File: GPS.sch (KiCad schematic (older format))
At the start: 2 parts

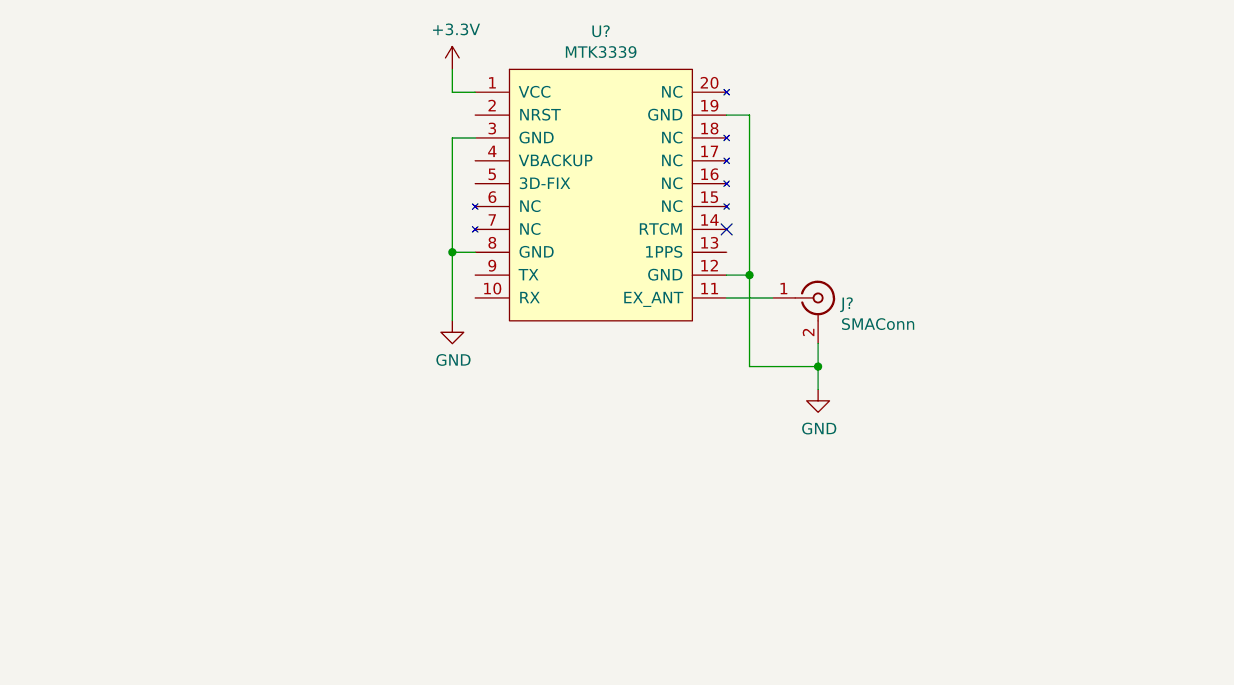
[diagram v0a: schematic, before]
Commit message: Adds connects all modules except for LEDs in schematics
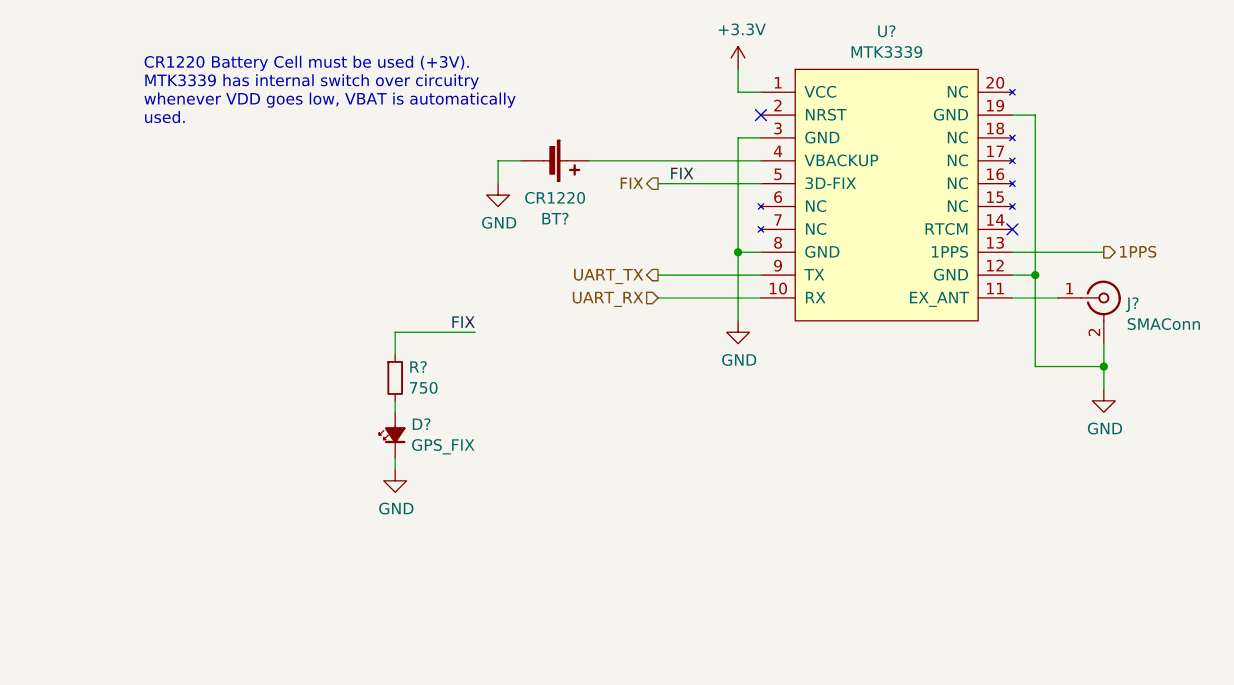
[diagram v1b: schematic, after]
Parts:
- added BT?: CR1220, Battery:BatteryHolder_Keystone_3000_1x12mm, symbol Device:Battery_Cell
- added D?: GPS_FIX, LED_SMD:LED_0805_2012Metric, symbol Device:LED_Small_ALT
- added R?: 750, Resistor_SMD:R_0805_2012Metric, symbol Device:R_Small
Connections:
- net GND: now also BT?.2 (-), D?.1 (K)
- net UART_RX: now reaches U?.10 (RX)
- net 1PPS: now reaches U?.13 (1PPS)
- net at U?.4 (VBACKUP): now also BT?.1 (+)
- net FIX: now reaches U?.5 (3D-FIX)
- net FIX: now also R?.1
- net UART_TX: now reaches U?.9 (TX)
- new net: D?.2 (A), R?.2
- no-connect marks 1 -> 2
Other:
- note added: "CR1220 Battery Cell must be used (+3V).\nMTK3339 has internal switch over circuitry\nwhenever VDD goes low, VBAT is automatically\nused."
- moved on the sheet: J?, U?
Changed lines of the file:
@@
 $Descr A4 11693 8268
 encoding utf-8
-Sheet 6 9
+Sheet 6 10
 Title ""
 Date ""
@@
 L Connector:Conn_Coaxial J?
 U 1 1 5FB64207
-P 4400 4650
-F 0 "J?" H 4500 4625 50  0000 L CNN
-F 1 "SMAConn" H 4500 4534 50  0000 L CNN
-F 2 "Connector_Coaxial:SMA_Amphenol_132203-12_Horizontal" H 4400 4650 50  0001 C CNN
-F 3 " ~" H 4400 4650 50  0001 C CNN
-	1    4400 4650
+P 5650 4650
+F 0 "J?" H 5750 4625 50  0000 L CNN
+F 1 "SMAConn" H 5750 4534 50  0000 L CNN
+F 2 "Connector_Coaxial:SMA_Amphenol_132203-12_Horizontal" H 5650 4650 50  0001 C CNN
+F 3 " ~" H 5650 4650 50  0001 C CNN
+	1    5650 4650
 	1    0    0    -1
 $EndComp
@@
 L utsvt-chips:MTK3339 U?
 U 1 1 5FB7A882
-P 3450 3650
-F 0 "U?" H 3450 3815 50  0000 C CNN
-F 1 "MTK3339" H 3450 3724 50  0000 C CNN
-F 2 "" H 3450 3650 50  0001 C CNN
-F 3 "" H 3450 3650 50  0001 C CNN
-	1    3450 3650
+P 4700 3650
+F 0 "U?" H 4700 3815 50  0000 C CNN
+F 1 "MTK3339" H 4700 3724 50  0000 C CNN
+F 2 "" H 4700 3650 50  0001 C CNN
+F 3 "" H 4700 3650 50  0001 C CNN
+	1    4700 3650
 	1    0    0    -1
 $EndComp
@@
 L power:GND #PWR?
 U 1 1 5FB7D6FC
-P 4400 5050
-F 0 "#PWR?" H 4400 4800 50  0001 C CNN
-F 1 "GND" H 4405 4877 50  0000 C CNN
-F 2 "" H 4400 5050 50  0001 C CNN
-F 3 "" H 4400 5050 50  0001 C CNN
-	1    4400 5050
+P 5650 5050
+F 0 "#PWR?" H 5650 4800 50  0001 C CNN
+F 1 "GND" H 5655 4877 50  0000 C CNN
+F 2 "" H 5650 5050 50  0001 C CNN
+F 3 "" H 5650 5050 50  0001 C CNN
+	1    5650 5050
 	1    0    0    -1
 $EndComp
 Wire Wire Line
-	4400 5050 4400 4950
+	5650 5050 5650 4950
 Wire Wire Line
-	4000 4650 4200 4650
+	5250 4650 5450 4650
 Wire Wire Line
-	4400 4950 4100 4950
+	5650 4950 5350 4950
 Wire Wire Line
-	4100 4950 4100 4550
+	5350 4950 5350 4550
 Wire Wire Line
-	4100 4550 4000 4550
-Connection ~ 4400 4950
+	5350 4550 5250 4550
+Connection ~ 5650 4950
 Wire Wire Line
-	4400 4950 4400 4850
+	5650 4950 5650 4850
 Wire Wire Line
-	4100 4550 4100 3850
+	5350 4550 5350 3850
 Wire Wire Line
-	4100 3850 4000 3850
-Connection ~ 4100 4550
-NoConn ~ 4000 4350
+	5350 3850 5250 3850
+Connection ~ 5350 4550
+NoConn ~ 5250 4350
 $Comp
 L power:+3.3V #PWR?
 U 1 1 5FB7FD95
-P 2800 3650
-F 0 "#PWR?" H 2800 3500 50  0001 C CNN
-F 1 "+3.3V" H 2815 3823 50  0000 C CNN
-F 2 "" H 2800 3650 50  0001 C CNN
-F 3 "" H 2800 3650 50  0001 C CNN
-	1    2800 3650
+P 4050 3650
+F 0 "#PWR?" H 4050 3500 50  0001 C CNN
+F 1 "+3.3V" H 4065 3823 50  0000 C CNN
+F 2 "" H 4050 3650 50  0001 C CNN
+F 3 "" H 4050 3650 50  0001 C CNN
+	1    4050 3650
 	1    0    0    -1
 $EndComp
 Wire Wire Line
-	2800 3650 2800 3750
+	4050 3650 4050 3750
 Wire Wire Line
-	2800 3750 2900 3750
+	4050 3750 4150 3750
 $Comp
 L power:GND #PWR?
 U 1 1 5FB808F2
-P 2800 4750
-F 0 "#PWR?" H 2800 4500 50  0001 C CNN
-F 1 "GND" H 2805 4577 50  0000 C CNN
-F 2 "" H 2800 4750 50  0001 C CNN
-F 3 "" H 2800 4750 50  0001 C CNN
-	1    2800 4750
+P 4050 4750
+F 0 "#PWR?" H 4050 4500 50  0001 C CNN
+F 1 "GND" H 4055 4577 50  0000 C CNN
+F 2 "" H 4050 4750 50  0001 C CNN
+F 3 "" H 4050 4750 50  0001 C CNN
+	1    4050 4750
 	1    0    0    -1
 $EndComp
 Wire Wire Line
-	2800 4750 2800 4450
+	4050 4750 4050 4450
 Wire Wire Line
-	2800 4450 2900 4450
+	4050 4450 4150 4450
 Wire Wire Line
-	2800 4450 2800 3950
+	4050 4450 4050 3950
 Wire Wire Line
-	2800 3950 2900 3950
-Connection ~ 2800 4450
+	4050 3950 4150 3950
+Connection ~ 4050 4450
+Text HLabel 5650 4450 2    50   Output ~ 0
+1PPS
+Wire Wire Line
+	5650 4450 5250 4450
+Text HLabel 3700 4550 0    50   Output ~ 0
+UART_TX
+Text HLabel 3700 4650 0    50   Input ~ 0
+UART_RX
+Wire Wire Line
+	3700 4650 4150 4650
+Wire Wire Line
+	4150 4550 3700 4550
+Text HLabel 3700 4150 0    50   Output ~ 0
+FIX
+Wire Wire Line
+	3700 4150 4150 4150
+NoConn ~ 4150 3850
+$Comp
+L Device:Battery_Cell BT?
+U 1 1 5F670A36
+P 3200 4050
+AR Path="/5F6F1E63/5F670A36" Ref="BT?"  Part="1"
+AR Path="/5F6EFD51/5F670A36" Ref="BT?"  Part="1"
+F 0 "BT?" V 3455 4100 50  0000 C CNN
+F 1 "CR1220" V 3364 4100 50  0000 C CNN
+F 2 "Battery:BatteryHolder_Keystone_3000_1x12mm" V 3200 4110 50  0001 C CNN
+F 3 "~" V 3200 4110 50  0001 C CNN
+	1    3200 4050
+	0    1    1    0
+$EndComp
+Wire Wire Line
+	3000 4050 3100 4050
+Text Notes 1450 3900 0    50   ~ 0
+CR1220 Battery Cell must be used (+3V).\nMTK3339 has internal switch over circuitry\nwhenever VDD goes low, VBAT is automatically\nused.
+Wire Wire Line
+	3400 4050 4150 4050
+$Comp
+L power:GND #PWR?
+U 1 1 5F67214A
+P 3000 4150
+F 0 "#PWR?" H 3000 3900 50  0001 C CNN
+F 1 "GND" H 3005 3977 50  0000 C CNN
+F 2 "" H 3000 4150 50  0001 C CNN
+F 3 "" H 3000 4150 50  0001 C CNN
+	1    3000 4150
+	1    0    0    -1
+$EndComp
+Wire Wire Line
+	3000 4150 3000 4050
+$Comp
+L Device:LED_Small_ALT D?
+U 1 1 5F6732BE
+P 2550 5250
+F 0 "D?" V 2596 5180 50  0000 R CNN
+F 1 "GPS_FIX" V 2505 5180 50  0000 R CNN
+F 2 "LED_SMD:LED_0805_2012Metric" V 2550 5250 50  0001 C CNN
+F 3 "~" V 2550 5250 50  0001 C CNN
+F 4 "Orange" V 2550 5250 50  0001 C CNN "Color"
+F 5 "1.8V" V 2550 5250 50  0001 C CNN "Vf"
+F 6 "2mA" V 2550 5250 50  0001 C CNN "If"
+F 7 "APT2012LSECK/J4-PRV" V 2550 5250 50  0001 C CNN "P/N"
+	1    2550 5250
+	0    -1   -1   0
+$EndComp
+$Comp
+L Device:R_Small R?
+U 1 1 5F6794C0
+P 2550 5000
+F 0 "R?" H 2609 5046 50  0000 L CNN
+F 1 "750" H 2609 4955 50  0000 L CNN
+F 2 "Resistor_SMD:R_0805_2012Metric" H 2550 5000 50  0001 C CNN
+F 3 "~" H 2550 5000 50  0001 C CNN
+	1    2550 5000
+	1    0    0    -1
+$EndComp
+Wire Wire Line
+	2550 5100 2550 5150
+Text Label 3750 4150 0    50   ~ 0
+FIX
+$Comp
+L power:GND #PWR?
+U 1 1 5F67AD77
+P 2550 5400
+F 0 "#PWR?" H 2550 5150 50  0001 C CNN
+F 1 "GND" H 2555 5227 50  0000 C CNN
+F 2 "" H 2550 5400 50  0001 C CNN
+F 3 "" H 2550 5400 50  0001 C CNN
+	1    2550 5400
+	1    0    0    -1
+$EndComp
+Wire Wire Line
+	2550 5350 2550 5400
+Wire Wire Line
+	2550 4900 2550 4800
+Wire Wire Line
+	2550 4800 2900 4800
+Text Label 2900 4800 2    50   ~ 0
+FIX
 $EndSCHEMATC

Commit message: Adds logic analyzer points and LEDs
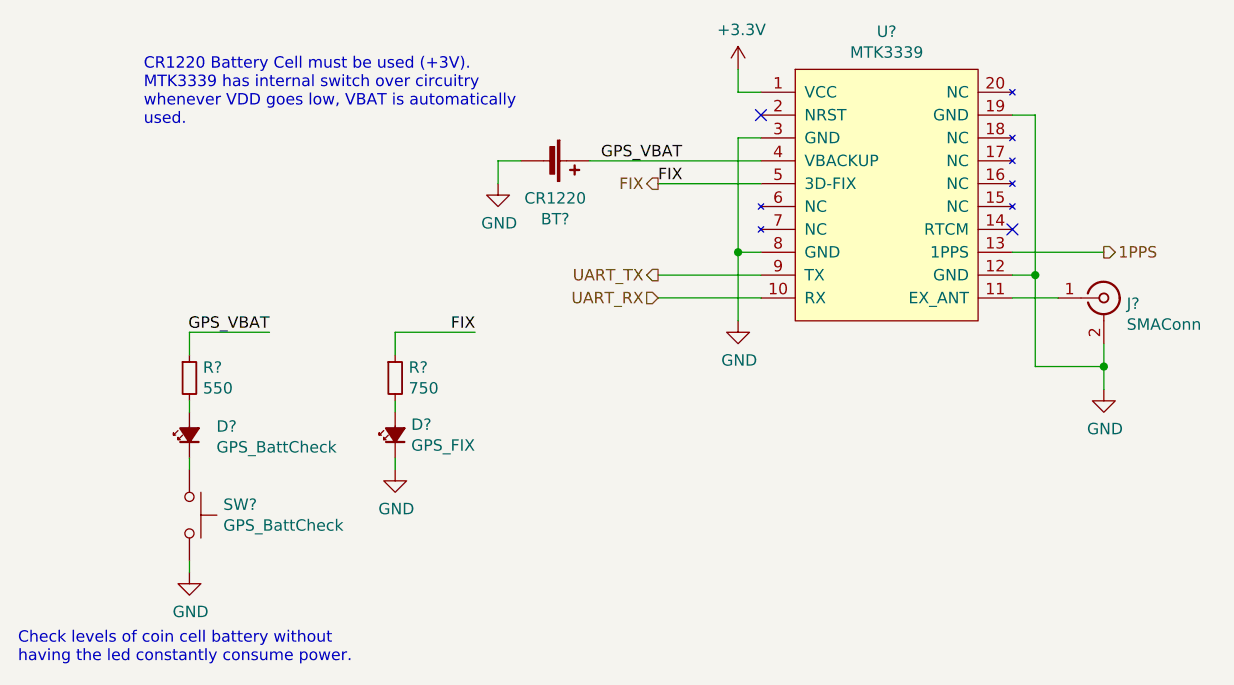
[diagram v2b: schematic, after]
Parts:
- added D?: GPS_BattCheck, LED_SMD:LED_0805_2012Metric, symbol Device:LED_Small_ALT
- added R?: 550, Resistor_SMD:R_0805_2012Metric, symbol Device:R_Small
- added SW?: GPS_BattCheck, Button_Switch_SMD:SW_SPST_B3SL-1002P, symbol Switch:SW_Push
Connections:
- net GND: now also SW?.2
- net GPS_VBAT: now reaches BT?.1 (+), U?.4 (VBACKUP)
- net GPS_VBAT: now also R?.1
- new net: D?.1 (K), SW?.1
- new net: D?.2 (A), R?.2
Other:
- note added: "Check levels of coin cell battery without\nhaving the led constantly consume power."
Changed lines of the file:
@@
 Wire Wire Line
 	2550 5100 2550 5150
-Text Label 3750 4150 0    50   ~ 0
+Text Label 3700 4150 0    50   ~ 0
 FIX
 $Comp
@@
 Text Label 2900 4800 2    50   ~ 0
 FIX
+Text Label 3450 4050 0    50   ~ 0
+GPS_VBAT
+Text Label 2000 4800 2    50   ~ 0
+GPS_VBAT
+$Comp
+L power:GND #PWR?
+U 1 1 5FD22D81
+P 1650 5850
+AR Path="/5F6CDFD6/5FD22D81" Ref="#PWR?"  Part="1"
+AR Path="/5F6EFD51/5FD22D81" Ref="#PWR?"  Part="1"
+F 0 "#PWR?" H 1650 5600 50  0001 C CNN
+F 1 "GND" H 1655 5677 50  0000 C CNN
+F 2 "" H 1650 5850 50  0001 C CNN
+F 3 "" H 1650 5850 50  0001 C CNN
+	1    1650 5850
+	1    0    0    -1
+$EndComp
+$Comp
+L Device:LED_Small_ALT D?
+U 1 1 5FD22D8B
+P 1650 5250
+AR Path="/5F6CDFD6/5FD22D8B" Ref="D?"  Part="1"
+AR Path="/5F6EFD51/5FD22D8B" Ref="D?"  Part="1"
+F 0 "D?" V 1688 5132 50  0000 R CNN
+F 1 "GPS_BattCheck" V 1597 5132 50  0000 R CNN
+F 2 "LED_SMD:LED_0805_2012Metric" H 1650 5250 50  0001 C CNN
+F 3 "~" H 1650 5250 50  0001 C CNN
+F 4 "Green" V 1650 5250 50  0001 C CNN "Color"
+F 5 "APTD2012LCGCK" V 1650 5250 50  0001 C CNN "P/N"
+F 6 "1.9V" V 1650 5250 50  0001 C CNN "Vf"
+F 7 "2mA" V 1650 5250 50  0001 C CNN "If"
+	1    1650 5250
+	0    -1   -1   0
+$EndComp
+Wire Wire Line
+	1650 5400 1650 5350
+Wire Wire Line
+	1650 4800 1650 4900
+Wire Wire Line
+	2000 4800 1650 4800
+$Comp
+L Device:R_Small R?
+U 1 1 5FD2598F
+P 1650 5000
+F 0 "R?" H 1709 5046 50  0000 L CNN
+F 1 "550" H 1709 4955 50  0000 L CNN
+F 2 "Resistor_SMD:R_0805_2012Metric" H 1650 5000 50  0001 C CNN
+F 3 "~" H 1650 5000 50  0001 C CNN
+	1    1650 5000
+	1    0    0    -1
+$EndComp
+Wire Wire Line
+	1650 5150 1650 5100
+Wire Wire Line
+	1650 5800 1650 5850
+Text Notes 900  6250 0    50   ~ 0
+Check levels of coin cell battery without\nhaving the led constantly consume power.
+$Comp
+L Switch:SW_Push SW?
+U 1 1 5FD394FE
+P 1650 5600
+AR Path="/5FD394FE" Ref="SW?"  Part="1"
+AR Path="/5F6EFD51/5FD394FE" Ref="SW?"  Part="1"
+F 0 "SW?" V 1604 5748 50  0000 L CNN
+F 1 "GPS_BattCheck" V 1695 5748 50  0000 L CNN
+F 2 "Button_Switch_SMD:SW_SPST_B3SL-1002P" H 1650 5800 50  0001 C CNN
+F 3 "~" H 1650 5800 50  0001 C CNN
+F 4 "EVQ-7Q203W or B3SL-1002P" V 1650 5600 50  0001 C CNN "P/N"
+	1    1650 5600
+	0    1    1    0
+$EndComp
 $EndSCHEMATC

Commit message: Initial layout of the Telemtry board.
The ethernet interface needs more work.
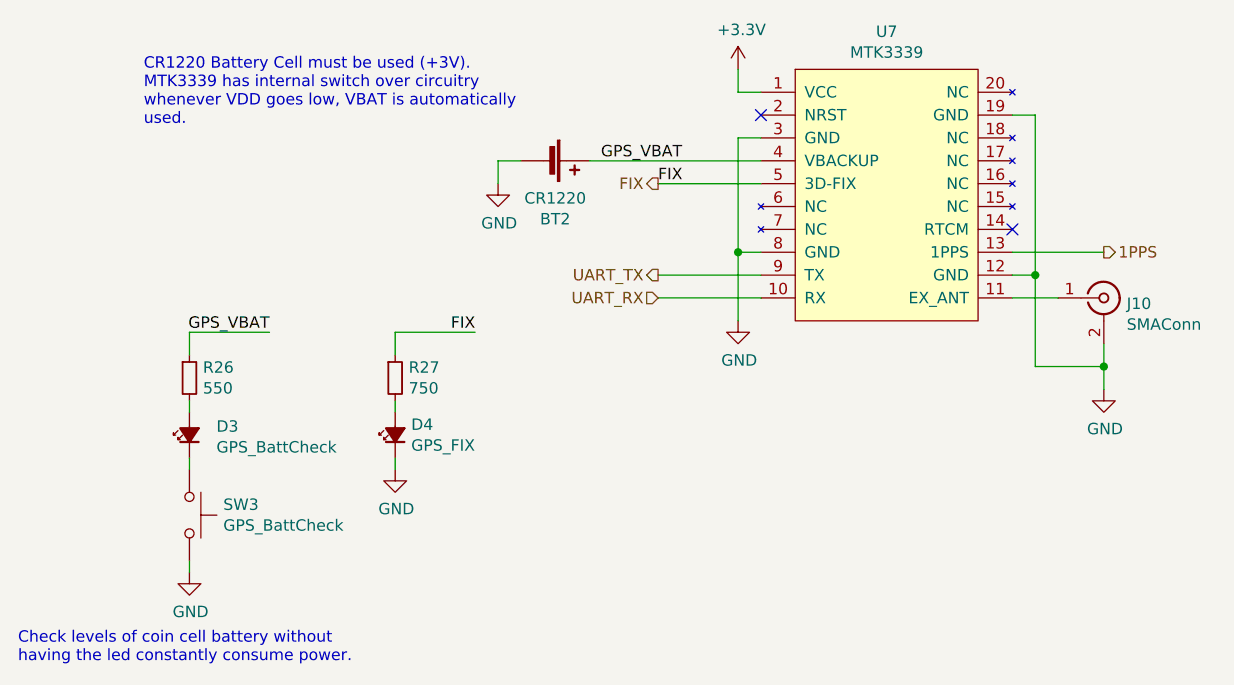
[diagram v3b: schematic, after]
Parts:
- U7: renamed from U?; footprint (none) -> UTSVT_Special:FGPMMOPA6H
- gave numbers to parts that had none: 7
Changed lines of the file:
@@
 $EndDescr
 $Comp
-L Connector:Conn_Coaxial J?
+L Connector:Conn_Coaxial J10
 U 1 1 5FB64207
 P 5650 4650
-F 0 "J?" H 5750 4625 50  0000 L CNN
+F 0 "J10" H 5750 4625 50  0000 L CNN
 F 1 "SMAConn" H 5750 4534 50  0000 L CNN
 F 2 "Connector_Coaxial:SMA_Amphenol_132203-12_Horizontal" H 5650 4650 50  0001 C CNN
@@
 $EndComp
 $Comp
-L utsvt-chips:MTK3339 U?
+L utsvt-chips:MTK3339 U7
 U 1 1 5FB7A882
 P 4700 3650
-F 0 "U?" H 4700 3815 50  0000 C CNN
+F 0 "U7" H 4700 3815 50  0000 C CNN
 F 1 "MTK3339" H 4700 3724 50  0000 C CNN
-F 2 "" H 4700 3650 50  0001 C CNN
+F 2 "UTSVT_Special:FGPMMOPA6H" H 4700 3650 50  0001 C CNN
 F 3 "" H 4700 3650 50  0001 C CNN
 	1    4700 3650
@@
 $EndComp
 $Comp
-L power:GND #PWR?
+L power:GND #PWR0154
 U 1 1 5FB7D6FC
 P 5650 5050
-F 0 "#PWR?" H 5650 4800 50  0001 C CNN
+F 0 "#PWR0154" H 5650 4800 50  0001 C CNN
 F 1 "GND" H 5655 4877 50  0000 C CNN
 F 2 "" H 5650 5050 50  0001 C CNN
@@
 NoConn ~ 5250 4350
 $Comp
-L power:+3.3V #PWR?
+L power:+3.3V #PWR0155
 U 1 1 5FB7FD95
 P 4050 3650
-F 0 "#PWR?" H 4050 3500 50  0001 C CNN
+F 0 "#PWR0155" H 4050 3500 50  0001 C CNN
 F 1 "+3.3V" H 4065 3823 50  0000 C CNN
 F 2 "" H 4050 3650 50  0001 C CNN
@@
 	4050 3750 4150 3750
 $Comp
-L power:GND #PWR?
+L power:GND #PWR0156
 U 1 1 5FB808F2
 P 4050 4750
-F 0 "#PWR?" H 4050 4500 50  0001 C CNN
+F 0 "#PWR0156" H 4050 4500 50  0001 C CNN
 F 1 "GND" H 4055 4577 50  0000 C CNN
 F 2 "" H 4050 4750 50  0001 C CNN
@@
 P 3200 4050
 AR Path="/5F6F1E63/5F670A36" Ref="BT?"  Part="1"
-AR Path="/5F6EFD51/5F670A36" Ref="BT?"  Part="1"
-F 0 "BT?" V 3455 4100 50  0000 C CNN
+AR Path="/5F6EFD51/5F670A36" Ref="BT2"  Part="1"
+F 0 "BT2" V 3455 4100 50  0000 C CNN
 F 1 "CR1220" V 3364 4100 50  0000 C CNN
 F 2 "Battery:BatteryHolder_Keystone_3000_1x12mm" V 3200 4110 50  0001 C CNN
@@
 	3400 4050 4150 4050
 $Comp
-L power:GND #PWR?
+L power:GND #PWR0157
 U 1 1 5F67214A
 P 3000 4150
-F 0 "#PWR?" H 3000 3900 50  0001 C CNN
+F 0 "#PWR0157" H 3000 3900 50  0001 C CNN
 F 1 "GND" H 3005 3977 50  0000 C CNN
 F 2 "" H 3000 4150 50  0001 C CNN
@@
 	3000 4150 3000 4050
 $Comp
-L Device:LED_Small_ALT D?
+L Device:LED_Small_ALT D4
 U 1 1 5F6732BE
 P 2550 5250
-F 0 "D?" V 2596 5180 50  0000 R CNN
+F 0 "D4" V 2596 5180 50  0000 R CNN
 F 1 "GPS_FIX" V 2505 5180 50  0000 R CNN
 F 2 "LED_SMD:LED_0805_2012Metric" V 2550 5250 50  0001 C CNN
@@
 $EndComp
 $Comp
-L Device:R_Small R?
+L Device:R_Small R27
 U 1 1 5F6794C0
 P 2550 5000
-F 0 "R?" H 2609 5046 50  0000 L CNN
+F 0 "R27" H 2609 5046 50  0000 L CNN
 F 1 "750" H 2609 4955 50  0000 L CNN
 F 2 "Resistor_SMD:R_0805_2012Metric" H 2550 5000 50  0001 C CNN
@@
 FIX
 $Comp
-L power:GND #PWR?
+L power:GND #PWR0158
 U 1 1 5F67AD77
 P 2550 5400
-F 0 "#PWR?" H 2550 5150 50  0001 C CNN
+F 0 "#PWR0158" H 2550 5150 50  0001 C CNN
 F 1 "GND" H 2555 5227 50  0000 C CNN
 F 2 "" H 2550 5400 50  0001 C CNN
@@
 P 1650 5850
 AR Path="/5F6CDFD6/5FD22D81" Ref="#PWR?"  Part="1"
-AR Path="/5F6EFD51/5FD22D81" Ref="#PWR?"  Part="1"
-F 0 "#PWR?" H 1650 5600 50  0001 C CNN
+AR Path="/5F6EFD51/5FD22D81" Ref="#PWR0159"  Part="1"
+F 0 "#PWR0159" H 1650 5600 50  0001 C CNN
 F 1 "GND" H 1655 5677 50  0000 C CNN
 F 2 "" H 1650 5850 50  0001 C CNN
@@
 P 1650 5250
 AR Path="/5F6CDFD6/5FD22D8B" Ref="D?"  Part="1"
-AR Path="/5F6EFD51/5FD22D8B" Ref="D?"  Part="1"
-F 0 "D?" V 1688 5132 50  0000 R CNN
+AR Path="/5F6EFD51/5FD22D8B" Ref="D3"  Part="1"
+F 0 "D3" V 1688 5132 50  0000 R CNN
 F 1 "GPS_BattCheck" V 1597 5132 50  0000 R CNN
 F 2 "LED_SMD:LED_0805_2012Metric" H 1650 5250 50  0001 C CNN
@@
 	2000 4800 1650 4800
 $Comp
-L Device:R_Small R?
+L Device:R_Small R26
 U 1 1 5FD2598F
 P 1650 5000
-F 0 "R?" H 1709 5046 50  0000 L CNN
+F 0 "R26" H 1709 5046 50  0000 L CNN
 F 1 "550" H 1709 4955 50  0000 L CNN
 F 2 "Resistor_SMD:R_0805_2012Metric" H 1650 5000 50  0001 C CNN
@@
 P 1650 5600
 AR Path="/5FD394FE" Ref="SW?"  Part="1"
-AR Path="/5F6EFD51/5FD394FE" Ref="SW?"  Part="1"
-F 0 "SW?" V 1604 5748 50  0000 L CNN
+AR Path="/5F6EFD51/5FD394FE" Ref="SW3"  Part="1"
+F 0 "SW3" V 1604 5748 50  0000 L CNN
 F 1 "GPS_BattCheck" V 1695 5748 50  0000 L CNN
 F 2 "Button_Switch_SMD:SW_SPST_B3SL-1002P" H 1650 5800 50  0001 C CNN
